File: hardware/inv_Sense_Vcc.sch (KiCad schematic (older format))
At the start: 5 parts, among them U1 ATtiny13A-SSU

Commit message: added a pull-up resistor to ATtiny reset pin
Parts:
- added R?: 10k, Resistor_SMD:R_0603_1608Metric_Pad1.05x0.95mm_HandSolder, symbol Device:R
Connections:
- net 3.3V: now also R?.1
- net ~RESET~: now also R?.2
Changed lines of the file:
@@
 	1    0    0    -1
 $EndComp
-Text HLabel 4700 4400 2    50   Input ~ 0
+Text HLabel 5800 4400 2    50   Input ~ 0
 ~RESET~
 Text HLabel 4700 3900 2    50   Input ~ 0
@@
 	4700 4300 4400 4300
 Wire Wire Line
-	4700 4400 4400 4400
+	5800 4400 5500 4400
 Text HLabel 4700 4200 2    50   Input ~ 0
 Sense_Vcc
@@
 Wire Wire Line
 	2000 3250 1600 3250
+$Comp
+L Device:R R?
+U 1 1 5C840859
+P 5500 4150
+AR Path="/5C840859" Ref="R?"  Part="1"
+AR Path="/5C33FF90/5C840859" Ref="R?"  Part="1"
+F 0 "R?" H 5570 4196 50  0000 L CNN
+F 1 "10k" H 5570 4105 50  0000 L CNN
+F 2 "Resistor_SMD:R_0603_1608Metric_Pad1.05x0.95mm_HandSolder" V 5430 4150 50  0001 C CNN
+F 3 "~" H 5500 4150 50  0001 C CNN
+	1    5500 4150
+	1    0    0    -1
+$EndComp
+Wire Wire Line
+	5500 4300 5500 4400
+Connection ~ 5500 4400
+Wire Wire Line
+	5500 4400 4400 4400
+Wire Wire Line
+	5500 4000 5500 3900
+Text GLabel 5500 3900 1    50   Input ~ 0
+3.3V
 $EndSCHEMATC

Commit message: Implement next hardware revision
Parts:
- removed TP2: Sense_Vcc, TestPoint:TestPoint_Keystone_5000-5004_Miniature, symbol Connector:TestPoint
- added R5: 4.7k, Resistor_SMD:R_0603_1608Metric_Pad1.05x0.95mm_HandSolder, symbol Device:R
- gave numbers to parts that had none: 1
- renumbered C1 to C2, D2 to D7, R2 to R6
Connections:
- net GND: now also R5.2
- net Sense_Vcc: now also R5.1; no longer U1.2 (PB3)
- net +12V_protected renamed +12V
- net inv_Sense_Vcc renamed PB4
- new net PB3: U1.2 (PB3)
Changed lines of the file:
@@
 $Descr A4 11693 8268
 encoding utf-8
-Sheet 2 7
+Sheet 2 8
 Title ""
 Date ""
@@
 P 1600 3100
 AR Path="/5C342FCB" Ref="R?"  Part="1"
-AR Path="/5C33FF90/5C342FCB" Ref="R2"  Part="1"
-F 0 "R2" H 1670 3146 50  0000 L CNN
+AR Path="/5C33FF90/5C342FCB" Ref="R6"  Part="1"
+F 0 "R6" H 1670 3146 50  0000 L CNN
 F 1 "4.7k" H 1670 3055 50  0000 L CNN
 F 2 "Resistor_SMD:R_0603_1608Metric_Pad1.05x0.95mm_HandSolder" V 1530 3100 50  0001 C CNN
@@
 P 1600 3400
 AR Path="/5C342FD2" Ref="D?"  Part="1"
-AR Path="/5C33FF90/5C342FD2" Ref="D2"  Part="1"
-F 0 "D2" V 1554 3479 50  0000 L CNN
+AR Path="/5C33FF90/5C342FD2" Ref="D7"  Part="1"
+F 0 "D7" V 1554 3479 50  0000 L CNN
 F 1 "Zener 3V3" V 1645 3479 50  0000 L CNN
 F 2 "Diode_SMD:D_SOD-123" H 1600 3400 50  0001 C CNN
@@
 P 1600 3550
 AR Path="/5C342FD9" Ref="#PWR?"  Part="1"
-AR Path="/5C33FF90/5C342FD9" Ref="#PWR013"  Part="1"
-F 0 "#PWR013" H 1600 3300 50  0001 C CNN
+AR Path="/5C33FF90/5C342FD9" Ref="#PWR019"  Part="1"
+F 0 "#PWR019" H 1600 3300 50  0001 C CNN
 F 1 "GND" H 1605 3377 50  0000 C CNN
 F 2 "" H 1600 3550 50  0001 C CNN
@@
 Connection ~ 1600 3250
 Wire Wire Line
-	2250 3250 2000 3250
-Wire Wire Line
 	1600 2800 1600 2950
 Text HLabel 2250 3250 2    50   Output ~ 0
 Sense_Vcc
 Text HLabel 1600 2800 1    50   Input ~ 0
-+12V_protected
++12V
 Text HLabel 4700 4300 2    50   Output ~ 0
-inv_Sense_Vcc
+PB4
 $Comp
 L power:GND #PWR?
@@
 P 3800 4800
 AR Path="/5C38F484" Ref="#PWR?"  Part="1"
-AR Path="/5C33FF90/5C38F484" Ref="#PWR014"  Part="1"
-F 0 "#PWR014" H 3800 4550 50  0001 C CNN
+AR Path="/5C33FF90/5C38F484" Ref="#PWR020"  Part="1"
+F 0 "#PWR020" H 3800 4550 50  0001 C CNN
 F 1 "GND" H 3805 4627 50  0000 C CNN
 F 2 "" H 3800 4800 50  0001 C CNN
@@
 	5800 4400 5500 4400
 Text HLabel 4700 4200 2    50   Input ~ 0
-Sense_Vcc
+PB3
 $Comp
-L Device:C C1
+L Device:C C2
 U 1 1 5C6051E1
 P 4200 3250
-F 0 "C1" H 4315 3296 50  0000 L CNN
+F 0 "C2" H 4315 3296 50  0000 L CNN
 F 1 "100nF" H 4315 3205 50  0000 L CNN
 F 2 "Capacitor_SMD:C_0603_1608Metric_Pad1.05x0.95mm_HandSolder" H 4238 3100 50  0001 C CNN
@@
 P 4200 3400
 AR Path="/5C6052C2" Ref="#PWR?"  Part="1"
-AR Path="/5C33FF90/5C6052C2" Ref="#PWR015"  Part="1"
-F 0 "#PWR015" H 4200 3150 50  0001 C CNN
+AR Path="/5C33FF90/5C6052C2" Ref="#PWR021"  Part="1"
+F 0 "#PWR021" H 4200 3150 50  0001 C CNN
 F 1 "GND" H 4205 3227 50  0000 C CNN
 F 2 "" H 4200 3400 50  0001 C CNN
@@
 	4700 4100 4400 4100
 $Comp
-L Connector:TestPoint TP2
-U 1 1 5C653726
-P 2000 3250
-F 0 "TP2" H 2050 3450 50  0000 L CNN
-F 1 "Sense_Vcc" H 2050 3350 50  0000 L CNN
-F 2 "TestPoint:TestPoint_Keystone_5000-5004_Miniature" H 2200 3250 50  0001 C CNN
-F 3 "~" H 2200 3250 50  0001 C CNN
-	1    2000 3250
-	1    0    0    -1
-$EndComp
-Connection ~ 2000 3250
-Wire Wire Line
-	2000 3250 1600 3250
-$Comp
 L Device:R R?
 U 1 1 5C840859
 P 5500 4150
 AR Path="/5C840859" Ref="R?"  Part="1"
-AR Path="/5C33FF90/5C840859" Ref="R?"  Part="1"
-F 0 "R?" H 5570 4196 50  0000 L CNN
+AR Path="/5C33FF90/5C840859" Ref="R7"  Part="1"
+F 0 "R7" H 5570 4196 50  0000 L CNN
 F 1 "10k" H 5570 4105 50  0000 L CNN
 F 2 "Resistor_SMD:R_0603_1608Metric_Pad1.05x0.95mm_HandSolder" V 5430 4150 50  0001 C CNN
@@
 Text GLabel 5500 3900 1    50   Input ~ 0
 3.3V
+$Comp
+L Device:R R?
+U 1 1 5C8BEFE2
+P 1300 3400
+AR Path="/5C8BEFE2" Ref="R?"  Part="1"
+AR Path="/5C33FF90/5C8BEFE2" Ref="R5"  Part="1"
+F 0 "R5" H 1370 3446 50  0000 L CNN
+F 1 "4.7k" H 1370 3355 50  0000 L CNN
+F 2 "Resistor_SMD:R_0603_1608Metric_Pad1.05x0.95mm_HandSolder" V 1230 3400 50  0001 C CNN
+F 3 "~" H 1300 3400 50  0001 C CNN
+	1    1300 3400
+	1    0    0    -1
+$EndComp
+$Comp
+L power:GND #PWR?
+U 1 1 5C8BF0DB
+P 1300 3550
+AR Path="/5C8BF0DB" Ref="#PWR?"  Part="1"
+AR Path="/5C33FF90/5C8BF0DB" Ref="#PWR018"  Part="1"
+F 0 "#PWR018" H 1300 3300 50  0001 C CNN
+F 1 "GND" H 1305 3377 50  0000 C CNN
+F 2 "" H 1300 3550 50  0001 C CNN
+F 3 "" H 1300 3550 50  0001 C CNN
+	1    1300 3550
+	1    0    0    -1
+$EndComp
+Wire Wire Line
+	1300 3250 1600 3250
+Wire Wire Line
+	1600 3250 2250 3250
 $EndSCHEMATC

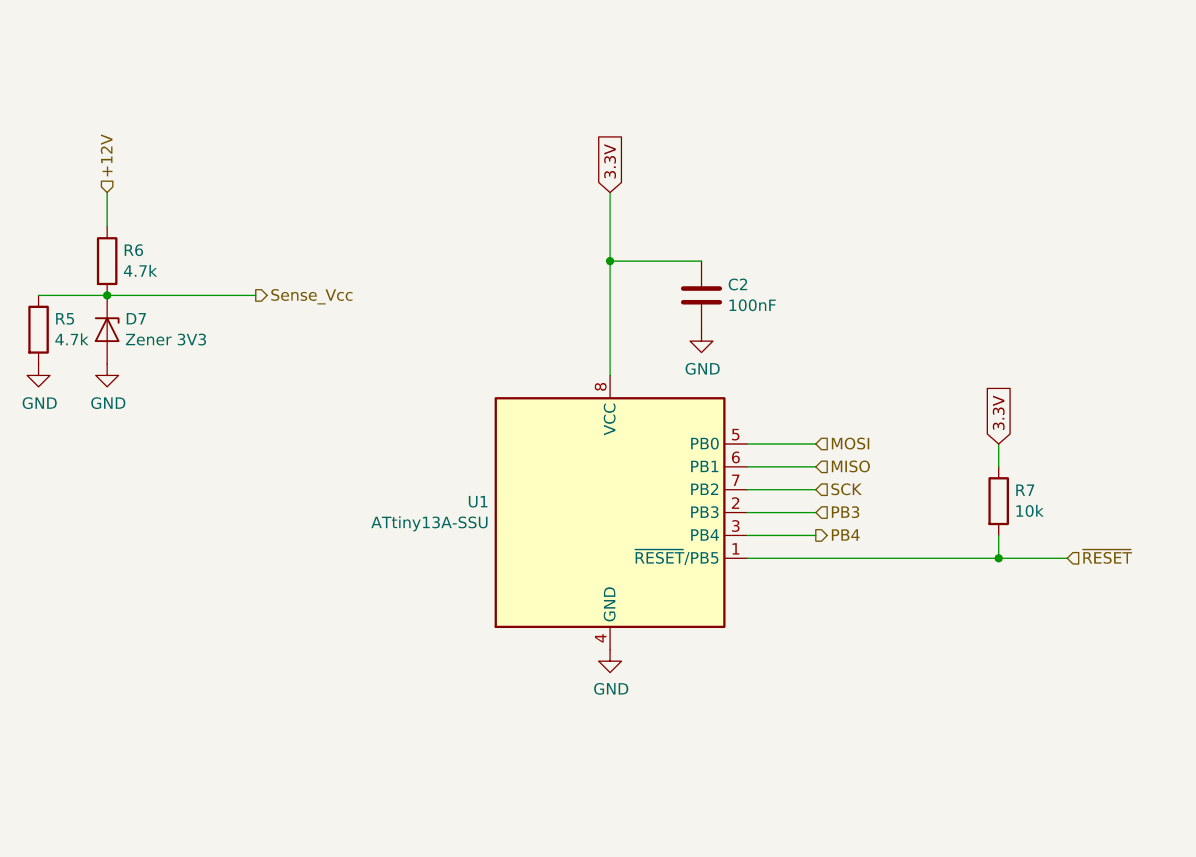
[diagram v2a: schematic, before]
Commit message: Changed to pure-serial topology. Changed to beefier mcu.
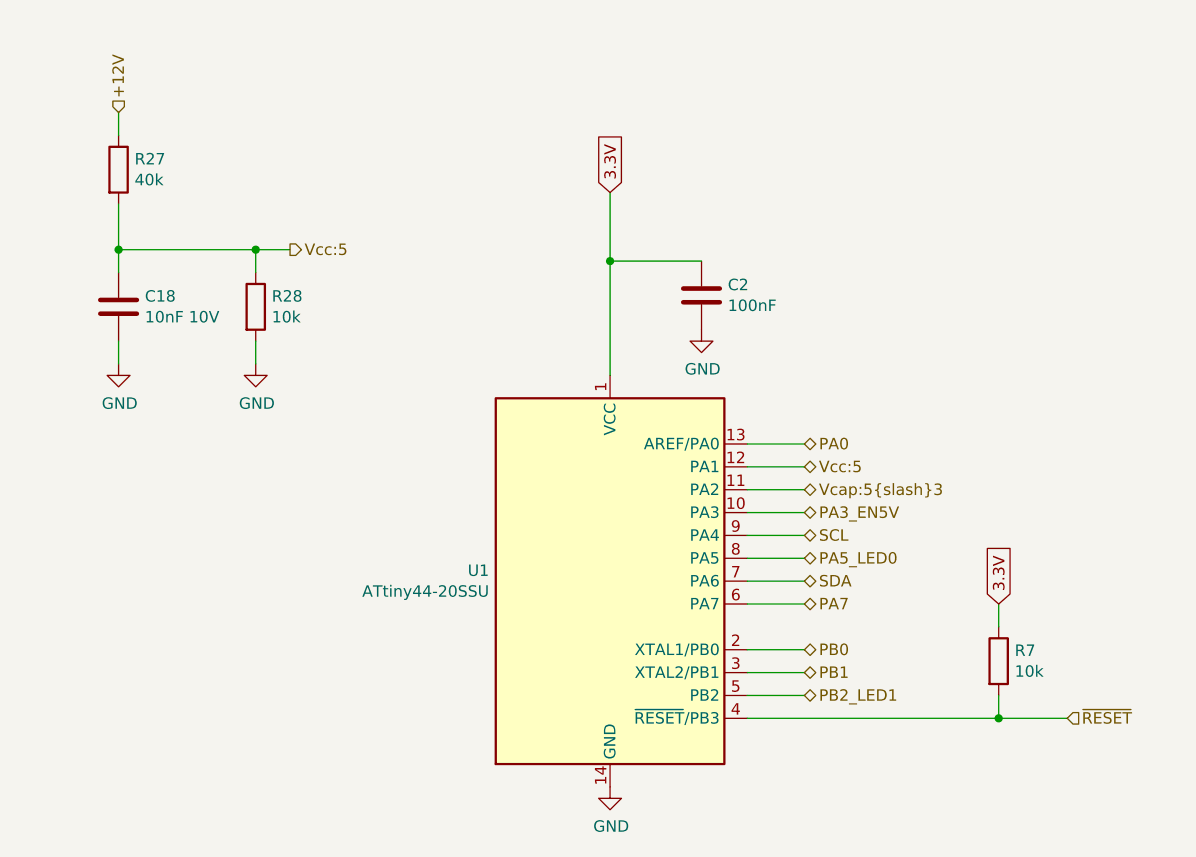
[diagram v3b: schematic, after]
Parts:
- removed D7: Zener 3V3, Diode_SMD:D_SOD-123, symbol Device:D_Zener
- removed R5, R6: 4.7k, Resistor_SMD:R_0603_1608Metric_Pad1.05x0.95mm_HandSolder, symbol Device:R
- removed U1: ATtiny13A-SSU, Package_SO:SOIC-8_3.9x4.9mm_P1.27mm, symbol MCU_Microchip_ATtiny:ATtiny13A-SSU
- added C18: 10nF 10V, Capacitor_SMD:C_0603_1608Metric_Pad1.05x0.95mm_HandSolder, symbol Device:C
- added R27: 40k, Resistor_SMD:R_0603_1608Metric_Pad1.05x0.95mm_HandSolder, symbol Device:R
- added R28: 10k, Resistor_SMD:R_0603_1608Metric_Pad1.05x0.95mm_HandSolder, symbol Device:R
- added U1: ATtiny44-20SSU, Package_SO:SOIC-14_3.9x8.7mm_P1.27mm, symbol MCU_Microchip_ATtiny:ATtiny44-20SSU
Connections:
- net +12V: now also R27.1
- net 3.3V: now also U1.1 (VCC)
- net GND: now also C18.2, R28.2, U1.14 (GND)
- net ~RESET~: now also U1.4 (~RESET~/PB3)
- new net PA0: U1.13 (AREF/PA0)
- new net PA3_EN5V: U1.10 (PA3)
- new net PA5_LED0: U1.8 (PA5)
- new net PA7: U1.6 (PA7)
- new net PB0: U1.2 (XTAL1/PB0)
- new net PB1: U1.3 (XTAL2/PB1)
- new net PB2_LED1: U1.5 (PB2)
- new net SCL: U1.9 (PA4)
- new net SDA: U1.7 (PA6)
- new net Vcap:5/3: U1.11 (PA2)
- new net Vcc:5: C18.1, R27.2, R28.1, U1.12 (PA1)
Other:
- moved on the sheet: R7

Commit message: Layout partially done before change of plans
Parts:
- added D4: BAT54C, Package_TO_SOT_SMD:SOT-23, symbol Diode:BAT54C
- R27: value 40k -> 50k
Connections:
- net 3.3V: now also D4.2; no longer C2.1, R7.1, U1.1 (VCC)
- net PA5_LED0 renamed PA5
- net PB1 renamed PB1_LED0
- net Vcap:5/3 renamed VcapS
- net Vcc:5 renamed V12:6
- new net 2.65V: D4.1
- new net ATT_Vcc: C2.1, D4.3, R7.1, U1.1 (VCC)
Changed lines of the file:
@@
 $Descr A4 11693 8268
 encoding utf-8
-Sheet 5 8
+Sheet 4 6
 Title ""
 Date ""
@@
 Comment3 ""
 Comment4 ""
+Comment5 ""
+Comment6 ""
+Comment7 ""
+Comment8 ""
+Comment9 ""
 $EndDescr
 $Comp
@@
 	1    0    0    -1
 $EndComp
-Text GLabel 3800 2800 1    50   Input ~ 0
+Text GLabel 4100 2600 2    50   Input ~ 0
 3.3V
 Wire Wire Line
-	3800 2800 3800 3100
+	3800 2800 3800 2900
 Text HLabel 5800 5100 2    50   Input ~ 0
 ~RESET~
@@
 Wire Wire Line
 	5500 5100 4400 5100
-Wire Wire Line
-	5500 4700 5500 4600
-Text GLabel 5500 4600 1    50   Input ~ 0
-3.3V
 $Comp
 L Device:R R?
@@
 AR Path="/5C33FF90/5CF4FF7C" Ref="R27"  Part="1"
 F 0 "R27" H 1720 2746 50  0000 L CNN
-F 1 "40k" H 1720 2655 50  0000 L CNN
+F 1 "50k" H 1720 2655 50  0000 L CNN
 F 2 "Resistor_SMD:R_0603_1608Metric_Pad1.05x0.95mm_HandSolder" V 1580 2700 50  0001 C CNN
 F 3 "~" H 1650 2700 50  0001 C CNN
@@
 $EndComp
 Text HLabel 2400 3050 2    50   Output ~ 0
-Vcc:5
+V12:6
 Wire Wire Line
 	1650 3050 1650 2850
@@
 	1650 3050 2250 3050
 Connection ~ 2250 3050
-$Comp
-L MCU_Microchip_ATtiny:ATtiny44-20SSU U1
-U 1 1 5D51A7F9
-P 3800 4500
-F 0 "U1" H 3271 4546 50  0000 R CNN
-F 1 "ATtiny44-20SSU" H 3271 4455 50  0000 R CNN
-F 2 "Package_SO:SOIC-14_3.9x8.7mm_P1.27mm" H 3800 4500 50  0001 C CIN
-F 3 "http://ww1.microchip.com/downloads/en/DeviceDoc/doc8006.pdf" H 3800 4500 50  0001 C CNN
-	1    3800 4500
-	1    0    0    -1
-$EndComp
 $Bitmap
 Pos 3650 6600
@@
 SCL
 Text HLabel 4650 4400 2    50   BiDi ~ 0
-PA5_LED0
+PA5
 Text HLabel 4650 4600 2    50   BiDi ~ 0
 PA7
 Text HLabel 4650 4200 2    50   BiDi ~ 0
 PA3_EN5V
-Text HLabel 4650 4100 2    50   BiDi ~ 0
-Vcap:5{slash}3
 Text HLabel 4650 4000 2    50   BiDi ~ 0
-Vcc:5
+V12:6
 Text HLabel 4650 3900 2    50   BiDi ~ 0
 PA0
@@
 PB0
 Text HLabel 4650 4900 2    50   BiDi ~ 0
-PB1
+PB1_LED0
 Text HLabel 4650 5000 2    50   BiDi ~ 0
 PB2_LED1
@@
 	4400 4000 4650 4000
 Wire Wire Line
-	4650 4100 4400 4100
-Wire Wire Line
 	4400 4200 4650 4200
 Wire Wire Line
@@
 Wire Wire Line
 	4650 5000 4400 5000
+$Comp
+L Diode:BAT54C D4
+U 1 1 5D59AF4D
+P 3800 2600
+F 0 "D4" H 3800 2825 50  0000 C CNN
+F 1 "BAT54C" H 3800 2734 50  0000 C CNN
+F 2 "Package_TO_SOT_SMD:SOT-23" H 3875 2725 50  0001 L CNN
+F 3 "http://www.diodes.com/_files/datasheets/ds11005.pdf" H 3720 2600 50  0001 C CNN
+	1    3800 2600
+	1    0    0    -1
+$EndComp
+Text GLabel 3500 2600 0    50   Input ~ 0
+2.65V
+Wire Wire Line
+	5500 2900 4850 2900
+Wire Wire Line
+	5500 2900 5500 4700
+Connection ~ 3800 2900
+Wire Wire Line
+	3800 2900 3800 3100
+Text HLabel 3800 3300 0    50   Input ~ 0
+ATT_Vcc
+$Comp
+L power:PWR_FLAG #FLG0103
+U 1 1 5D5BF9CE
+P 4850 2900
+F 0 "#FLG0103" H 4850 2975 50  0001 C CNN
+F 1 "PWR_FLAG" H 4850 3073 50  0000 C CNN
+F 2 "" H 4850 2900 50  0001 C CNN
+F 3 "~" H 4850 2900 50  0001 C CNN
+	1    4850 2900
+	1    0    0    -1
+$EndComp
+Connection ~ 4850 2900
+Wire Wire Line
+	4850 2900 3800 2900
+$Comp
+L MCU_Microchip_ATtiny:ATtiny44-20SSU U1
+U 1 1 5D62E779
+P 3800 4500
+F 0 "U1" H 3271 4546 50  0000 R CNN
+F 1 "ATtiny44-20SSU" H 3271 4455 50  0000 R CNN
+F 2 "Package_SO:SOIC-14_3.9x8.7mm_P1.27mm" H 3800 4500 50  0001 C CIN
+F 3 "http://ww1.microchip.com/downloads/en/DeviceDoc/doc8006.pdf" H 3800 4500 50  0001 C CNN
+	1    3800 4500
+	1    0    0    -1
+$EndComp
+Text HLabel 4650 4100 2    50   Input ~ 0
+VcapS
+Wire Wire Line
+	4650 4100 4400 4100
 $EndSCHEMATC

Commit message: revE ready for production
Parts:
- C18: value 10nF 10V -> 100nF
- R27: value 50k -> 51k
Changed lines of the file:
@@
 $Descr A4 11693 8268
 encoding utf-8
-Sheet 4 6
+Sheet 4 7
 Title ""
 Date ""
@@
 AR Path="/5C33FF90/5CF4FF7C" Ref="R27"  Part="1"
 F 0 "R27" H 1720 2746 50  0000 L CNN
-F 1 "50k" H 1720 2655 50  0000 L CNN
+F 1 "51k" H 1720 2655 50  0000 L CNN
 F 2 "Resistor_SMD:R_0603_1608Metric_Pad1.05x0.95mm_HandSolder" V 1580 2700 50  0001 C CNN
 F 3 "~" H 1650 2700 50  0001 C CNN
@@
 P 1650 3300
 F 0 "C18" H 1765 3346 50  0000 L CNN
-F 1 "10nF 10V" H 1765 3255 50  0000 L CNN
+F 1 "100nF" H 1765 3255 50  0000 L CNN
 F 2 "Capacitor_SMD:C_0603_1608Metric_Pad1.05x0.95mm_HandSolder" H 1688 3150 50  0001 C CNN
 F 3 "~" H 1650 3300 50  0001 C CNN

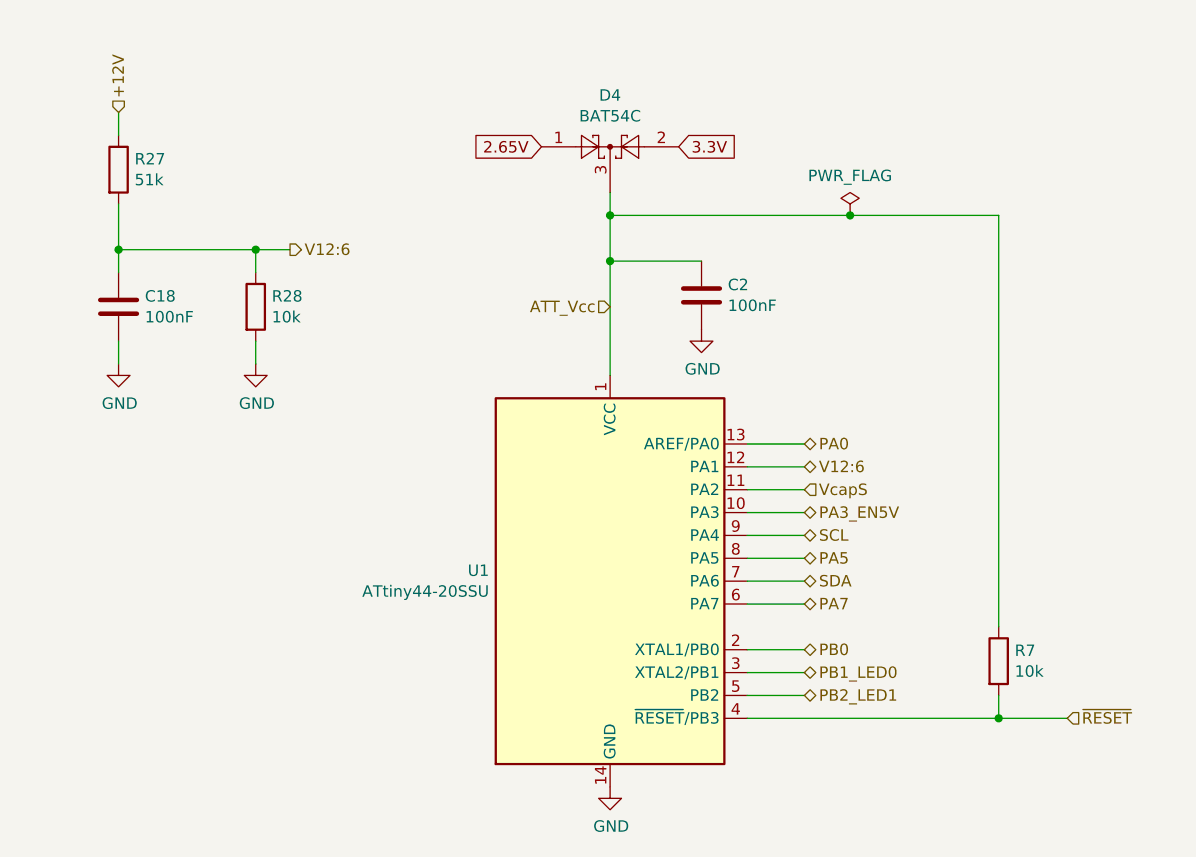
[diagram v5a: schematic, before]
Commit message: Add ENIN trace to the PCB. Change input voltage dividers for 1.1V ref.
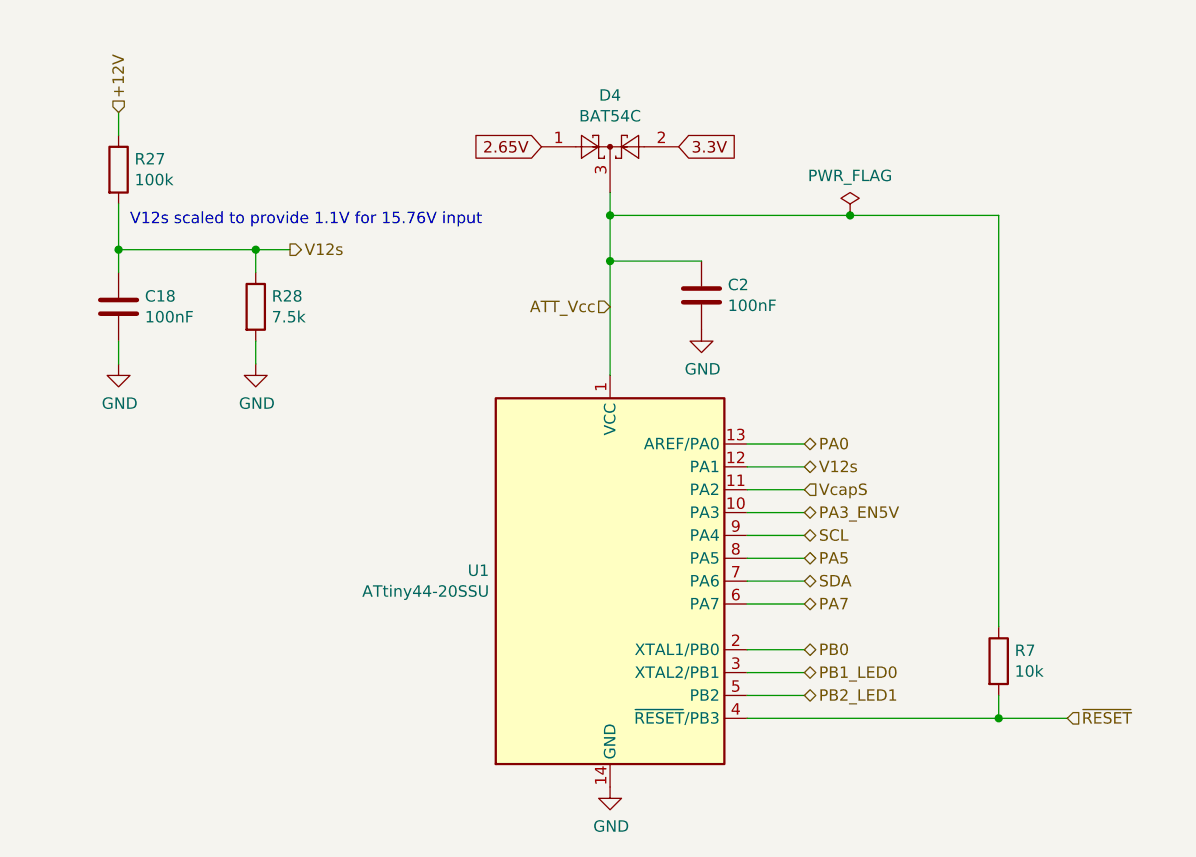
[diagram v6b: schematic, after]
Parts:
- R27: value 51k -> 100k
- R28: value 10k -> 7.5k
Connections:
- net V12:6 renamed V12s
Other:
- note added: "V12s scaled to provide 1.1V for 15.76V input"
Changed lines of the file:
@@
 AR Path="/5C33FF90/5CF4FF7C" Ref="R27"  Part="1"
 F 0 "R27" H 1720 2746 50  0000 L CNN
-F 1 "51k" H 1720 2655 50  0000 L CNN
+F 1 "100k" H 1720 2655 50  0000 L CNN
 F 2 "Resistor_SMD:R_0603_1608Metric_Pad1.05x0.95mm_HandSolder" V 1580 2700 50  0001 C CNN
 F 3 "~" H 1650 2700 50  0001 C CNN
@@
 $EndComp
 Text HLabel 2400 3050 2    50   Output ~ 0
-V12:6
+V12s
 Wire Wire Line
 	1650 3050 1650 2850
@@
 AR Path="/5C33FF90/5CFB31B2" Ref="R28"  Part="1"
 F 0 "R28" H 2320 3346 50  0000 L CNN
-F 1 "10k" H 2320 3255 50  0000 L CNN
+F 1 "7.5k" H 2320 3255 50  0000 L CNN
 F 2 "Resistor_SMD:R_0603_1608Metric_Pad1.05x0.95mm_HandSolder" V 2180 3300 50  0001 C CNN
 F 3 "~" H 2250 3300 50  0001 C CNN
@@
 PA3_EN5V
 Text HLabel 4650 4000 2    50   BiDi ~ 0
-V12:6
+V12s
 Text HLabel 4650 3900 2    50   BiDi ~ 0
 PA0
@@
 Wire Wire Line
 	4650 4100 4400 4100
+Text Notes 1700 2950 0    50   ~ 0
+V12s scaled to provide 1.1V for 15.76V input
 $EndSCHEMATC
